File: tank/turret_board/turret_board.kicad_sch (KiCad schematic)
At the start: 13 parts, among them U1 LD1117, U2 pixart_ir, Y1 Crystal_4pin

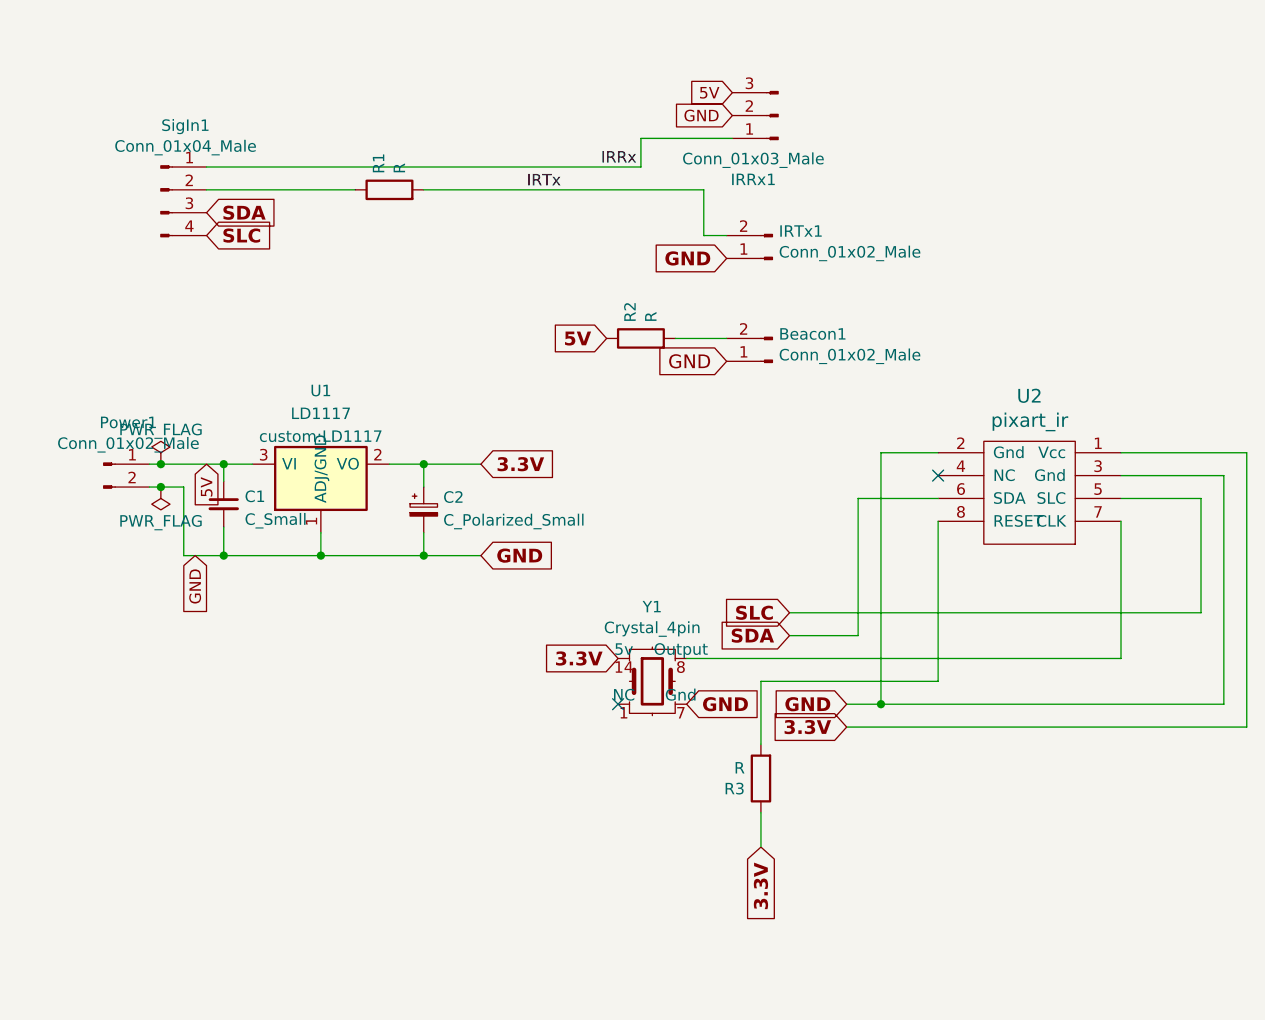
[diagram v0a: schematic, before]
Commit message: Turret Board v0.10: add connector for second I²C device
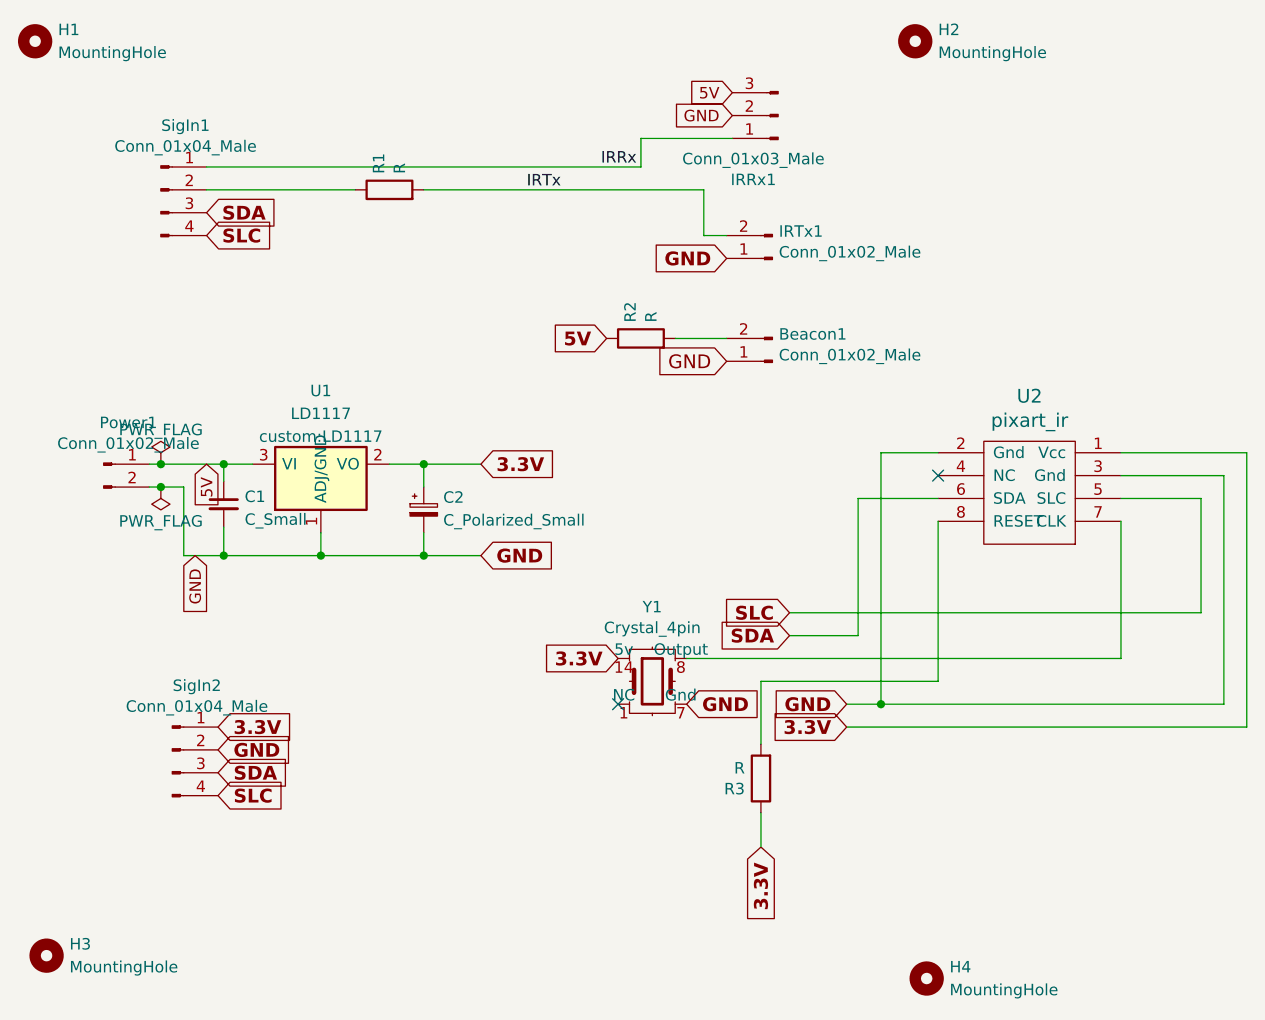
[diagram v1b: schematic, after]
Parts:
- added H1, H2, H3, H4: MountingHole, symbol Mechanical:MountingHole
- added SigIn2: Conn_01x04_Male, custom:JST_EH_B4B-EH-A_1x04_P2.50mm_Vertical, symbol custom:Conn_01x04_Male
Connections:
- net 3.3V: now also SigIn2.1 (Pin_1)
- net GND: now also SigIn2.2 (Pin_2)
- net SDA: now also SigIn2.3 (Pin_3)
- net SLC: now also SigIn2.4 (Pin_4)

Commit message: minor changes for turret board v0.11
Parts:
- H1, H2, H3, H4: footprint (none) -> MountingHole:MountingHole_2.2mm_M2
- renumbered SigIn2 to Distance1
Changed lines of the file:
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@@
 			)
 		)
-		(property "Footprint" ""
+		(property "Footprint" "MountingHole:MountingHole_2.2mm_M2"
 			(at 116.84 30.48 0)
 			(effects
@@
 			)
 		)
-		(property "Footprint" ""
+		(property "Footprint" "MountingHole:MountingHole_2.2mm_M2"
 			(at 19.05 30.48 0)
 			(effects
@@
 			)
 		)
-		(property "Footprint" ""
+		(property "Footprint" "MountingHole:MountingHole_2.2mm_M2"
 			(at 20.32 132.08 0)
 			(effects
@@
 			)
 		)
-		(property "Footprint" ""
+		(property "Footprint" "MountingHole:MountingHole_2.2mm_M2"
 			(at 118.11 134.62 0)
 			(effects
@@
 		(on_board yes)
 		(dnp no)
-		(property "Reference" "SigIn2"
+		(property "Reference" "Distance1"
 			(at 37.0332 102.0826 0)
 			(effects
@@
 			(project "turret_board"
 				(path "/1276d934-8177-4be4-bcd5-a48ef615db4e"
-					(reference "SigIn2")
-					(unit 1)
-				)
+					(reference "Distance1")
+					(unit 1)
+				)
